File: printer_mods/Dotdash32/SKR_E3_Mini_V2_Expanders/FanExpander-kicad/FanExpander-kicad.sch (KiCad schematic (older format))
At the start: 18 parts, among them J1 Conn_01x05, J2 Conn_01x01, J3 Conn_01x02, J4 Conn_01x01, J5 Conn_01x02, Q1 IRLZ34N, Q2 IRLZ34N

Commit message: feat: new fan expander using EXP1 header
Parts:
- removed C1: 10uF, symbol ME218_BaseLib:Cap
- removed D1, D2: LED, symbol ME218_BaseLib:LED
- removed J1: Conn_01x05, symbol Connector_Generic:Conn_01x05
- removed J2, J4: Conn_01x01, symbol Connector_Generic:Conn_01x01
- removed J3, J5: Conn_01x02, symbol Connector_Generic:Conn_01x02
- removed Q1, Q2: IRLZ34N, Package_TO_SOT_THT:TO-220-3_Vertical, symbol Transistor_FET:IRLZ34N
- removed R1, R5: 100R, symbol ME218_BaseLib:Res1
- removed R2, R6: 10k, symbol ME218_BaseLib:Res1
- removed R3, R7: 560R, symbol ME218_BaseLib:Res1
- removed R4, R8: 0R, symbol ME218_BaseLib:Res1
- added C1, C2: 10uF, symbol Device:C
- added D1, D2: CG0603MLC, symbol Device:D_TVS
- added D3, D4, D5, D6, D7, D8: LED, symbol Device:LED
- added F1: Polyfuse-2A, symbol Device:Polyfuse
- added F2: Fuse-5A, symbol Device:Fuse
- added F3: Polyfuse-1A, symbol Device:Polyfuse
- added J1, J10, J13, J14, J17, J18, J4, J8, J9: Conn_01x02, symbol Connector_Generic:Conn_01x02
- added J11, J12, J15, J16, J6, J7: Conn_01x03, symbol Connector_Generic:Conn_01x03
- added J2: Screw_Terminal_01x02, symbol Connector:Screw_Terminal_01x02
- added J3: Conn_02x05_Odd_Even, symbol Connector_Generic:Conn_02x05_Odd_Even
- added J5: Conn_01x01, symbol Connector_Generic:Conn_01x01
- added Q1, Q2, Q3, Q4, Q5: IRLML6344, symbol Device:Q_NMOS_GSD
- added R1, R4: 4.7k, symbol Device:R_US
- added R10, R15, R16, R5, R9: 100k, symbol Device:R_US
- added R11, R12, R17, R18, R6: 100R, symbol Device:R_US
- added R13, R14, R2, R3, R7, R8: 560R, symbol Device:R_US
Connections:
- net labels added: +24V, +3.3V, FAN1_Drive, FAN2_Drive, FAN3_Drive, FAN4, FAN4_Drive, FAN5, FAN5_Drive, FAN6, FAN6_Drive, TH2, TH3
- wire segments 45 -> 167
- no-connect marks 0 -> 1
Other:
- note added: "3.3V \nfrom SKR"
- note added: "Controls/Supply"
- note added: "EXP1 from SKR"
- note added: "External Voltage Bus"
- note added: "FAN1 - Passthrough"
- note added: "FAN1 from SKR"
- note added: "Fan Outputs"
- note added: "Fan2 - PB5"
- note added: "Fan3 - PB8"
- note added: "Fan4 - PA15"
- note added: "Fan5 - PB9"
- note added: "Fan6 - PB15"
- note added: "PB5 | PA15\nTX1/PA9 | RST\nRX1/PA10 | PB9\nPB8 | PB15\nGND | +5V"
- note added: "TH2 - PA9"
- note added: "TH3 - PA10"
- note added: "Thermistor Inputs"
- note removed: "LED always uses 5V \nfor consistent brightness"
- note removed: "PC14\nGND\nPA1\n+5V\nGND"
- note removed: "Remove 0 Ohm resistor \nand use PTH to inject new fan voltage"
- note removed: "Voltage Selector"

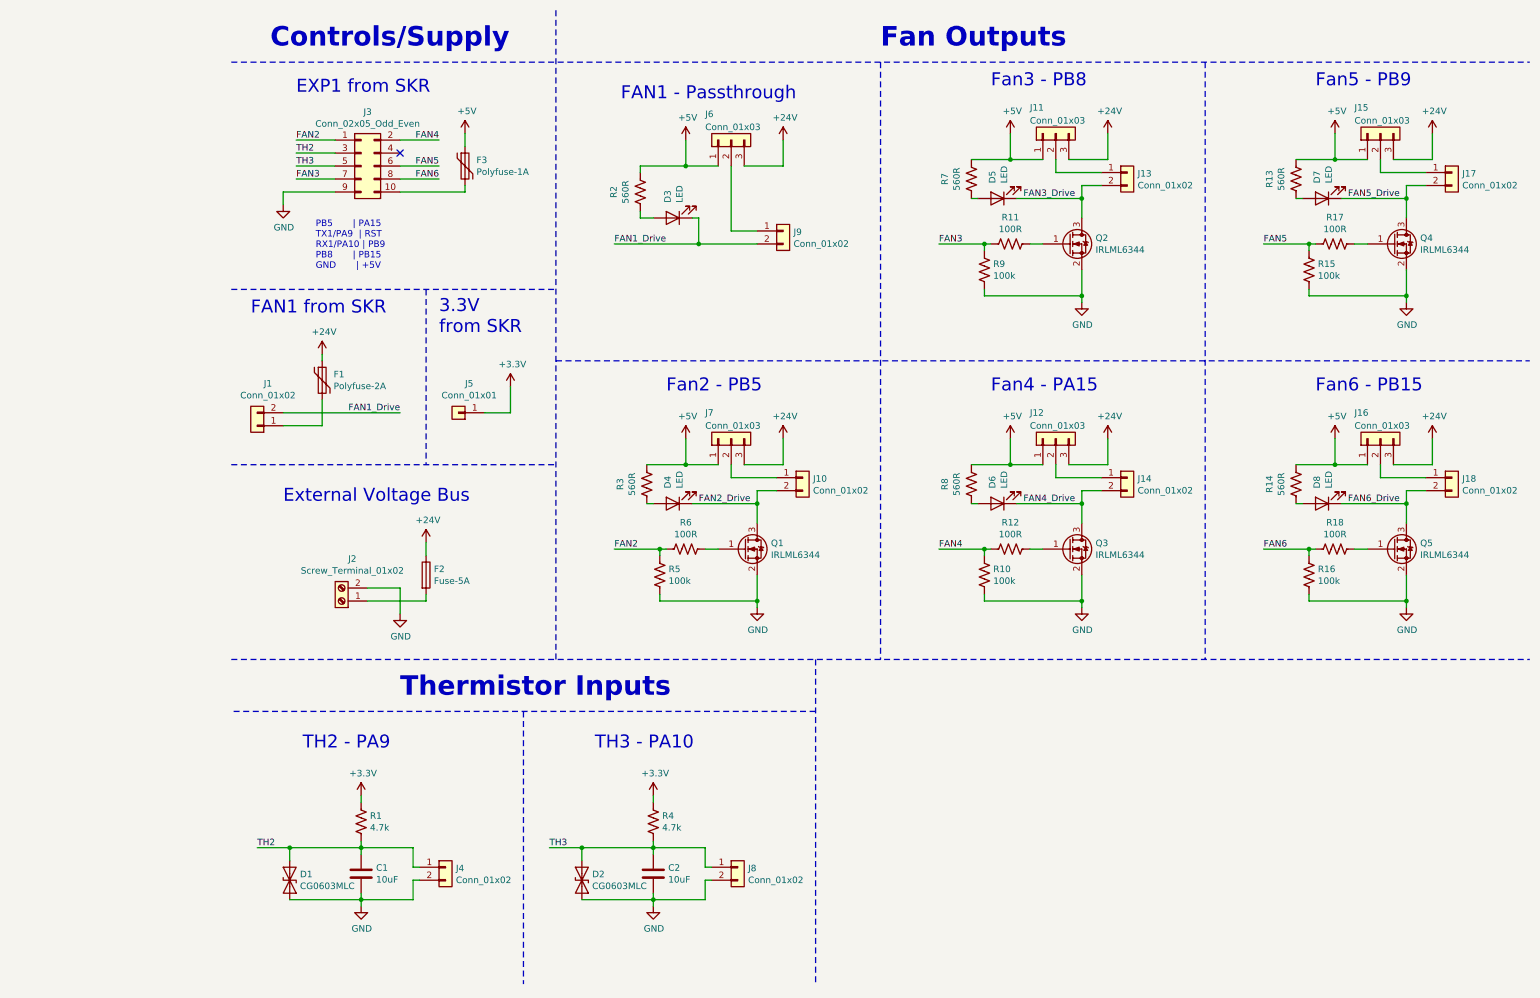
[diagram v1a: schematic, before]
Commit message: feat: init footprints, rename connectors per use
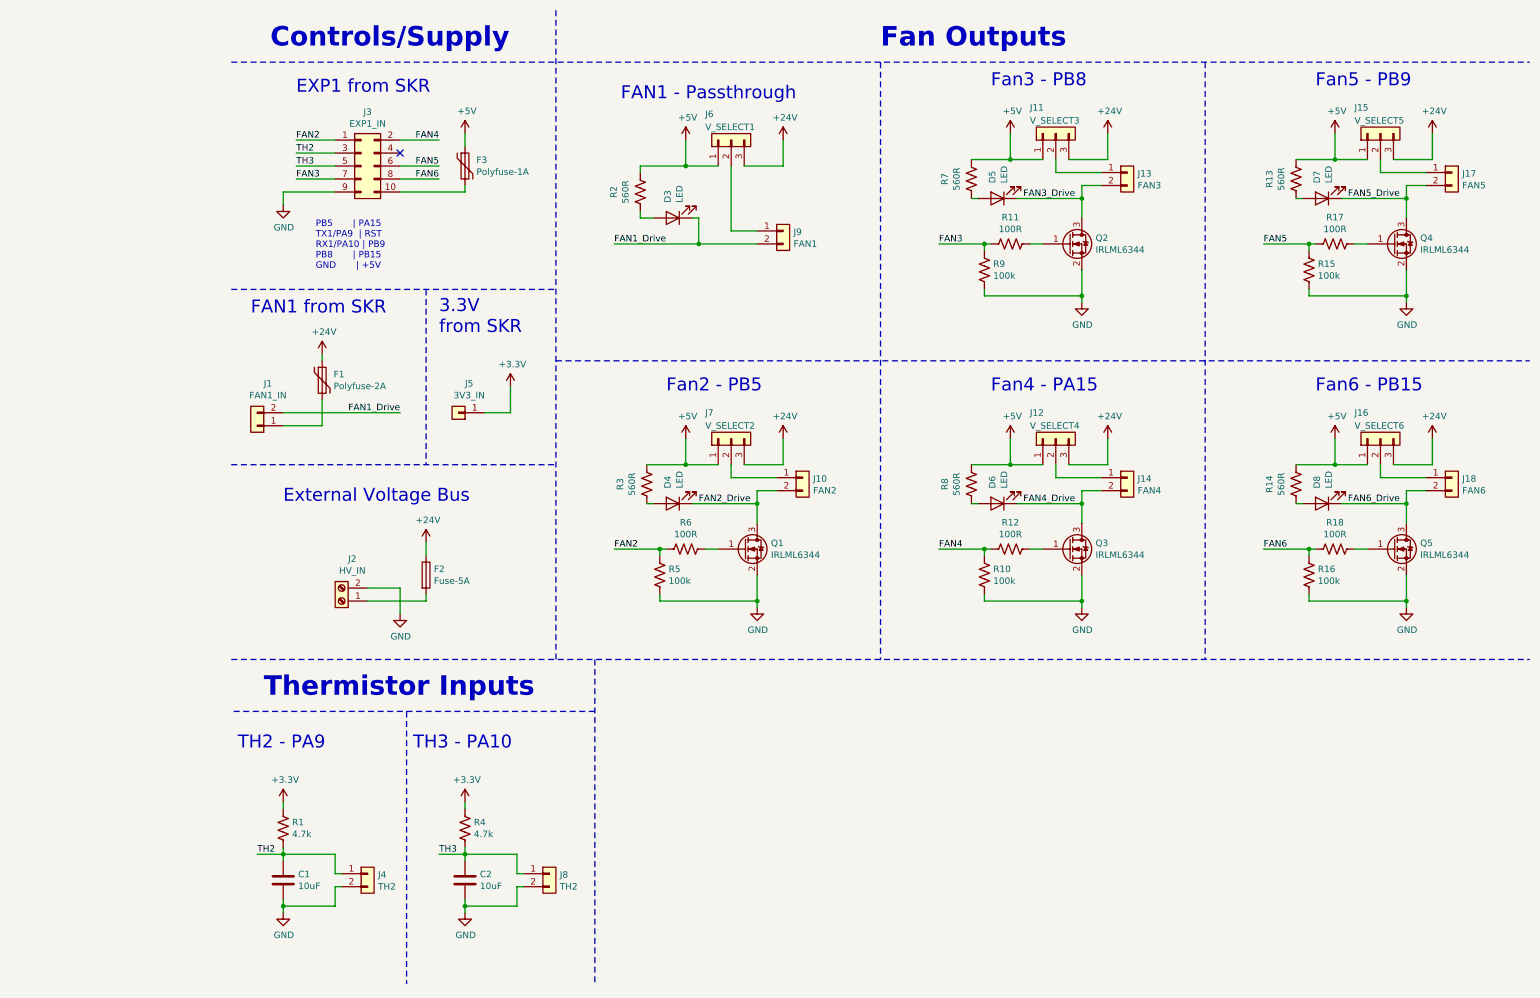
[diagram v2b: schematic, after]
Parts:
- removed D1, D2: CG0603MLC, symbol Device:D_TVS
- C1, C2: footprint (none) -> Capacitors_SMD:C_0805
- D3, D4, D5, D6, D7, D8: footprint (none) -> LEDs:LED_0603_HandSoldering
- F1, F3: footprint (none) -> Fuse_Holders_and_Fuses:Fuse_SMD1206_HandSoldering
- F2: footprint (none) -> Fuse_Holders_and_Fuses:BladeFuse-CarType
- J1: value Conn_01x02 -> FAN1_IN; footprint (none) -> Connectors_JST:JST_XH_B02B-XH-A_02x2.50mm_Straight
- J10: value Conn_01x02 -> FAN2; footprint (none) -> Connectors_JST:JST_XH_B02B-XH-A_02x2.50mm_Straight
- J11: value Conn_01x03 -> V_SELECT3; footprint (none) -> Pin_Headers:Pin_Header_Straight_1x03_Pitch2.54mm
- J12: value Conn_01x03 -> V_SELECT4; footprint (none) -> Pin_Headers:Pin_Header_Straight_1x03_Pitch2.54mm
- J13: value Conn_01x02 -> FAN3; footprint (none) -> Connectors_JST:JST_XH_B02B-XH-A_02x2.50mm_Straight
- J14: value Conn_01x02 -> FAN4; footprint (none) -> Connectors_JST:JST_XH_B02B-XH-A_02x2.50mm_Straight
- J15: value Conn_01x03 -> V_SELECT5; footprint (none) -> Pin_Headers:Pin_Header_Straight_1x03_Pitch2.54mm
- J16: value Conn_01x03 -> V_SELECT6; footprint (none) -> Pin_Headers:Pin_Header_Straight_1x03_Pitch2.54mm
- J17: value Conn_01x02 -> FAN5; footprint (none) -> Connectors_JST:JST_XH_B02B-XH-A_02x2.50mm_Straight
- J18: value Conn_01x02 -> FAN6; footprint (none) -> Connectors_JST:JST_XH_B02B-XH-A_02x2.50mm_Straight
- J2: value Screw_Terminal_01x02 -> HV_IN; footprint (none) -> Connectors_Terminal_Blocks:TerminalBlock_bornier-2_P5.08mm
- J3: value Conn_02x05_Odd_Even -> EXP1_IN; footprint (none) -> Pin_Headers:Pin_Header_Straight_2x05_Pitch2.54mm
- J4, J8: value Conn_01x02 -> TH2; footprint (none) -> Connectors_JST:JST_XH_B02B-XH-A_02x2.50mm_Straight
- J5: value Conn_01x01 -> 3V3_IN; footprint (none) -> Pin_Headers:Pin_Header_Straight_1x01_Pitch2.54mm
- J6: value Conn_01x03 -> V_SELECT1; footprint (none) -> Pin_Headers:Pin_Header_Straight_1x03_Pitch2.54mm
- J7: value Conn_01x03 -> V_SELECT2; footprint (none) -> Pin_Headers:Pin_Header_Straight_1x03_Pitch2.54mm
- J9: value Conn_01x02 -> FAN1; footprint (none) -> Connectors_JST:JST_XH_B02B-XH-A_02x2.50mm_Straight
- Q1, Q2, Q3, Q4, Q5: footprint (none) -> TO_SOT_Packages_SMD:SOT-23
- R1, R10, R11, R12, R13, R14, R15, R16, R17, R18, R2, R3, R4, R5, R6, R7, R8, R9: footprint (none) -> Resistors_SMD:R_0603_HandSoldering
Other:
- moved on the sheet: C1, C2, J4, J8, R1, R4

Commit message: test: initial layout, trying different mosfet arrs
testing different arragnments of Mosfets and associated
hardware, seeing the best routing and labelling way.
Trying to keep the designators on the board, which takes up space,
but in general i think i need to make things more sparse.
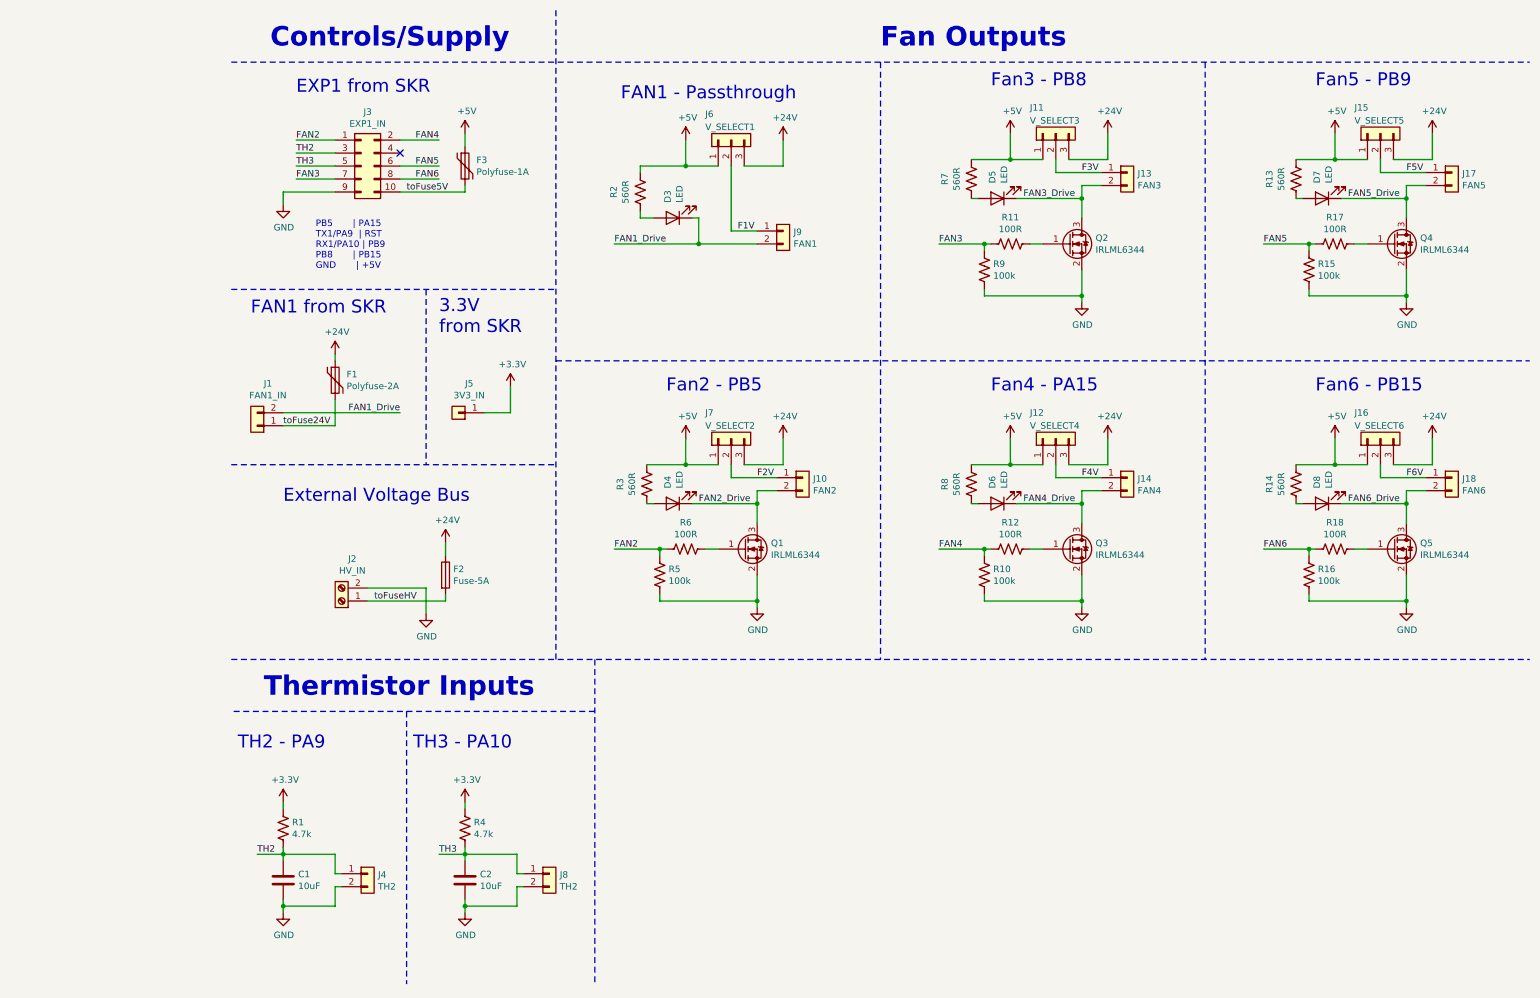
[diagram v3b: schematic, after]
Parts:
- J3: footprint Pin_Headers:Pin_Header_Straight_2x05_Pitch2.54mm -> Connectors_Multicomp:Multicomp_MC9A12-1034_2x05x2.54mm_Straight
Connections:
- net toFuse5V: now reaches F3.2, J3.10 (Pin_10)
- net toFuse24V: now reaches F1.2, J1.1 (Pin_1)
- net toFuseHV: now reaches F2.2, J2.1 (Pin_1)
- net F1V: now reaches J6.2 (Pin_2), J9.1 (Pin_1)
- net F2V: now reaches J10.1 (Pin_1), J7.2 (Pin_2)
- net F3V: now reaches J11.2 (Pin_2), J13.1 (Pin_1)
- net F4V: now reaches J12.2 (Pin_2), J14.1 (Pin_1)
- net F5V: now reaches J15.2 (Pin_2), J17.1 (Pin_1)
- net F6V: now reaches J16.2 (Pin_2), J18.1 (Pin_1)
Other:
- moved on the sheet: F1, F2
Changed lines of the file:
@@
 F 0 "J3" H 1550 2117 50  0000 C CNN
 F 1 "EXP1_IN" H 1550 2026 50  0000 C CNN
-F 2 "Pin_Headers:Pin_Header_Straight_2x05_Pitch2.54mm" H 1500 1700 50  0001 C CNN
+F 2 "Connectors_Multicomp:Multicomp_MC9A12-1034_2x05x2.54mm_Straight" H 1500 1700 50  0001 C CNN
 F 3 "~" H 1500 1700 50  0001 C CNN
 	1    1500 1700
@@
 L power:+24V #PWR0103
 U 1 1 61C19F25
-P 1200 3150
-F 0 "#PWR0103" H 1200 3000 50  0001 C CNN
-F 1 "+24V" H 1215 3323 50  0000 C CNN
-F 2 "" H 1200 3150 50  0001 C CNN
-F 3 "" H 1200 3150 50  0001 C CNN
-	1    1200 3150
-	1    0    0    -1
-$EndComp
-Wire Wire Line
-	900  3700 1200 3700
+P 1300 3150
+F 0 "#PWR0103" H 1300 3000 50  0001 C CNN
+F 1 "+24V" H 1315 3323 50  0000 C CNN
+F 2 "" H 1300 3150 50  0001 C CNN
+F 3 "" H 1300 3150 50  0001 C CNN
+	1    1300 3150
+	1    0    0    -1
+$EndComp
+Wire Wire Line
+	900  3700 1300 3700
 Wire Wire Line
 	900  3600 1800 3600
@@
 L Device:Polyfuse F1
 U 1 1 61C26288
-P 1200 3350
-F 0 "F1" H 1288 3396 50  0000 L CNN
-F 1 "Polyfuse-2A" H 1288 3305 50  0000 L CNN
-F 2 "Fuse_Holders_and_Fuses:Fuse_SMD1206_HandSoldering" H 1250 3150 50  0001 L CNN
-F 3 "~" H 1200 3350 50  0001 C CNN
-	1    1200 3350
+P 1300 3350
+F 0 "F1" H 1388 3396 50  0000 L CNN
+F 1 "Polyfuse-2A" H 1388 3305 50  0000 L CNN
+F 2 "Fuse_Holders_and_Fuses:Fuse_SMD1206_HandSoldering" H 1350 3150 50  0001 L CNN
+F 3 "~" H 1300 3350 50  0001 C CNN
+	1    1300 3350
 	1    0    0    -1
 $EndComp
@@
 	2300 1450 2300 1550
 Wire Wire Line
-	1200 3700 1200 3500
-Wire Wire Line
-	1200 3200 1200 3150
+	1300 3700 1300 3500
+Wire Wire Line
+	1300 3200 1300 3150
 $Comp
 L Device:Fuse F2
 U 1 1 61C36434
-P 2000 4850
-F 0 "F2" H 2060 4896 50  0000 L CNN
-F 1 "Fuse-5A" H 2060 4805 50  0000 L CNN
-F 2 "Fuse_Holders_and_Fuses:BladeFuse-CarType" V 1930 4850 50  0001 C CNN
-F 3 "~" H 2000 4850 50  0001 C CNN
-	1    2000 4850
+P 2150 4850
+F 0 "F2" H 2210 4896 50  0000 L CNN
+F 1 "Fuse-5A" H 2210 4805 50  0000 L CNN
+F 2 "Fuse_Holders_and_Fuses:BladeFuse-CarType" V 2080 4850 50  0001 C CNN
+F 3 "~" H 2150 4850 50  0001 C CNN
+	1    2150 4850
 	1    0    0    -1
 $EndComp
@@
 L power:GND #PWR03
 U 1 1 61C3BCC5
-P 1800 5150
-F 0 "#PWR03" H 1800 4900 50  0001 C CNN
-F 1 "GND" H 1805 4977 50  0000 C CNN
-F 2 "" H 1800 5150 50  0001 C CNN
-F 3 "" H 1800 5150 50  0001 C CNN
-	1    1800 5150
-	1    0    0    -1
-$EndComp
-Wire Wire Line
-	1550 5050 2000 5050
-Wire Wire Line
-	2000 5050 2000 5000
-Wire Wire Line
-	1550 4950 1800 4950
-Wire Wire Line
-	1800 4950 1800 5150
-Wire Wire Line
-	2000 4700 2000 4600
+P 2000 5150
+F 0 "#PWR03" H 2000 4900 50  0001 C CNN
+F 1 "GND" H 2005 4977 50  0000 C CNN
+F 2 "" H 2000 5150 50  0001 C CNN
+F 3 "" H 2000 5150 50  0001 C CNN
+	1    2000 5150
+	1    0    0    -1
+$EndComp
+Wire Wire Line
+	1550 5050 2150 5050
+Wire Wire Line
+	2150 5050 2150 5000
+Wire Wire Line
+	1550 4950 2000 4950
+Wire Wire Line
+	2000 4950 2000 5150
+Wire Wire Line
+	2150 4700 2150 4600
 $Comp
 L power:+24V #PWR04
 U 1 1 61C3AFF9
-P 2000 4600
-F 0 "#PWR04" H 2000 4450 50  0001 C CNN
-F 1 "+24V" H 2015 4773 50  0000 C CNN
-F 2 "" H 2000 4600 50  0001 C CNN
-F 3 "" H 2000 4600 50  0001 C CNN
-	1    2000 4600
+P 2150 4600
+F 0 "#PWR04" H 2150 4450 50  0001 C CNN
+F 1 "+24V" H 2165 4773 50  0000 C CNN
+F 2 "" H 2150 4600 50  0001 C CNN
+F 3 "" H 2150 4600 50  0001 C CNN
+	1    2150 4600
 	1    0    0    -1
 $EndComp
@@
 Wire Wire Line
 	2100 7000 2300 7000
+Text Label 4400 2200 0    50   ~ 0
+F1V
+Text Label 4550 4100 0    50   ~ 0
+F2V
+Text Label 7050 1750 0    50   ~ 0
+F3V
+Text Label 7050 4100 0    50   ~ 0
+F4V
+Text Label 9550 1750 0    50   ~ 0
+F5V
+Text Label 9550 4100 0    50   ~ 0
+F6V
+Text Label 900  3700 0    50   ~ 0
+toFuse24V
+Text Label 1600 5050 0    50   ~ 0
+toFuseHV
+Text Label 1850 1900 0    50   ~ 0
+toFuse5V
 $EndSCHEMATC
